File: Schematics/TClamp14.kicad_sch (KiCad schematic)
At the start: 1 part, among them J1 Conn_02x07_Counter_Clockwise

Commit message: Schematic Finished.
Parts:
- removed J1: Conn_02x07_Counter_Clockwise, symbol Connector_Generic:Conn_02x07_Counter_Clockwise
- added D1: LED_Small, LED_SMD:LED_0603_1608Metric, symbol Device:LED_Small
- added J1: FTSH-107-01-L-DV-K-A, FTSH-107-01-L-DV-K-A:SAMTEC_FTSH-107-01-L-DV-K-A, symbol TClamps:FTSH-107-01-L-DV-K-A
- added J2: Conn_02x07_Odd_Even, Connector_PinHeader_1.27mm:PinHeader_2x07_P1.27mm_Vertical, symbol Connector_Generic:Conn_02x07_Odd_Even
- added R1: 330, Resistor_SMD:R_0603_1608Metric, symbol Device:R_Small
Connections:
- new net: D1.2 (A), R1.2
- new net: J1.02, J2.2 (Pin_2)
- new net: J1.04, J2.4 (Pin_4)
- new net: J1.06, J2.6 (Pin_6)
- new net: J1.08, J2.8 (Pin_8)
- new net: J1.10, J2.10 (Pin_10)
- new net: J1.12, J2.12 (Pin_12)
- new net: J1.14, J2.14 (Pin_14)
- new net 1: J1.01, J2.1 (Pin_1)
- new net 11: J1.11, J2.11 (Pin_11)
- new net 13: J1.13, J2.13 (Pin_13)
- new net 3: J1.03, J2.3 (Pin_3), R1.1
- new net 7: J1.07, J2.7 (Pin_7)
- new net 9: J1.09, J2.9 (Pin_9)
- new net VSS: D1.1 (K), J1.05, J2.5 (Pin_5)
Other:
- note added: "STDC14 Style"

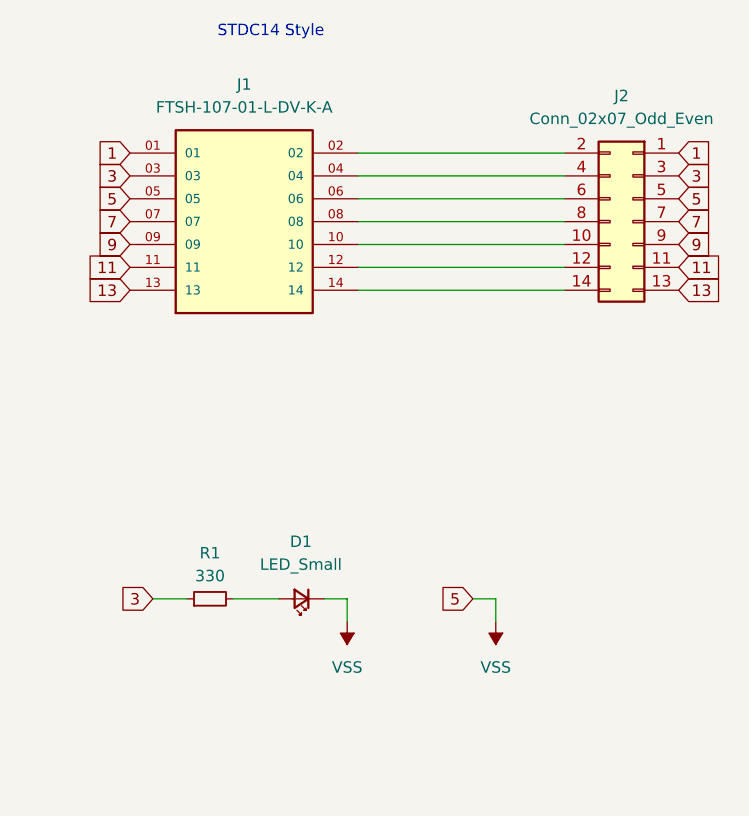
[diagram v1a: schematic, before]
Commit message: Decide on standard and started routing
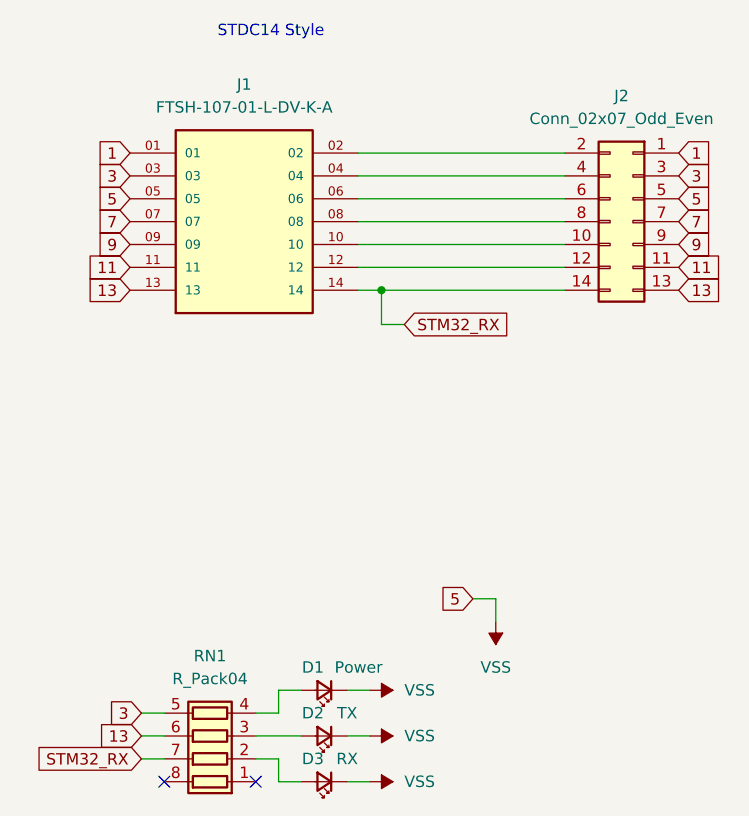
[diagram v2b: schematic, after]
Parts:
- removed R1: 330, Resistor_SMD:R_0603_1608Metric, symbol Device:R_Small
- added D2: TX, LED_SMD:LED_0603_1608Metric, symbol Device:LED_Small
- added D3: RX, LED_SMD:LED_0603_1608Metric, symbol Device:LED_Small
- added RN1: R_Pack04, Resistor_SMD:R_Array_Convex_4x0603, symbol Device:R_Pack04
- D1: value LED_Small -> Power
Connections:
- net 13: now also RN1.6 (R3.2)
- net 3: now also RN1.5 (R4.2)
- net VSS: now also D2.1 (K), D3.1 (K)
- net at D1.2 (A): now also RN1.4 (R4.1)
- net STM32_RX: now reaches J1.14, J2.14 (Pin_14)
- net STM32_RX: now also RN1.7 (R2.2)
- new net: D3.2 (A), RN1.2 (R2.1)
- new net: D2.2 (A), RN1.3 (R3.1)
- no-connect marks 0 -> 2
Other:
- moved on the sheet: D1
